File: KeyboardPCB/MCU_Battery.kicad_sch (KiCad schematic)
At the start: 23 parts, among them U1 ATmega32U4-M, U2 TPS61222DCK, U3 MCP73831-2-OT, Y1 XRCGB16M000FXN02R0

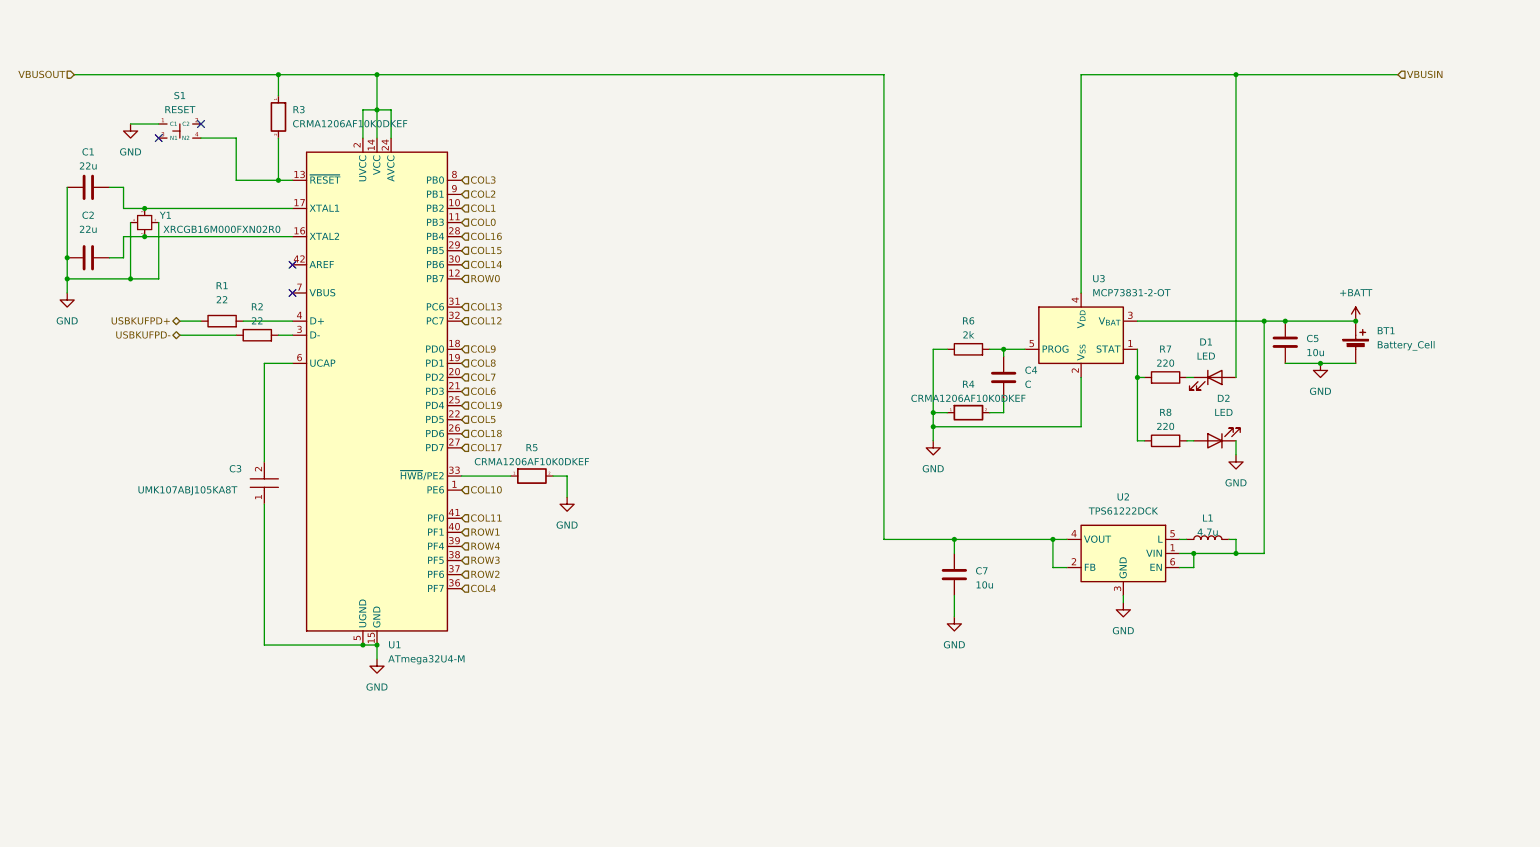
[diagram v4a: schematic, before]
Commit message: Added Symbols and placed them
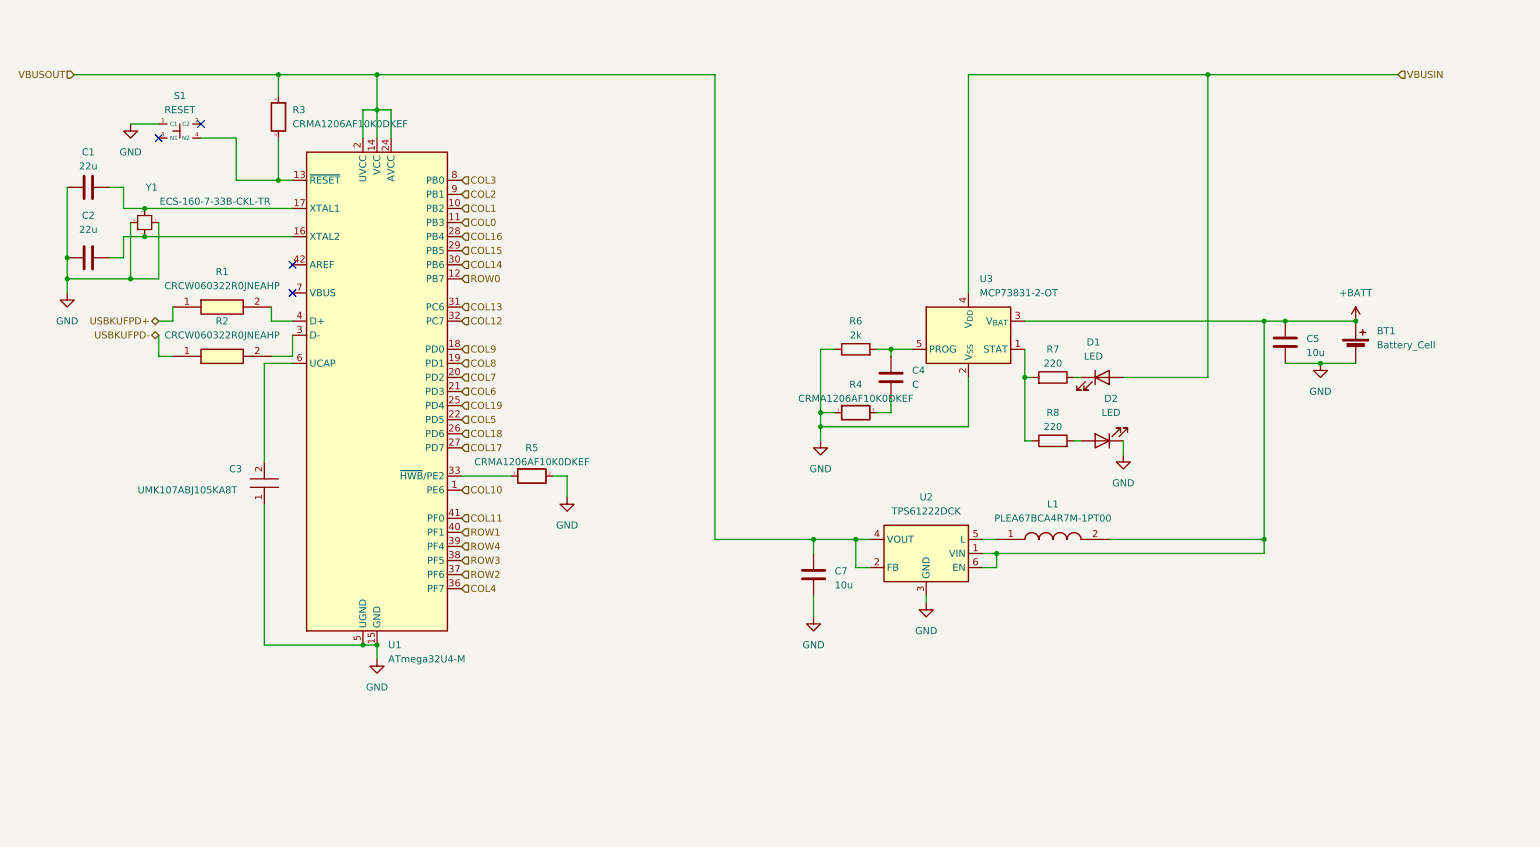
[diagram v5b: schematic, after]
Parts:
- removed L1: 4.7u, symbol Device:L
- removed R1, R2: 22, symbol Device:R
- removed Y1: XRCGB16M000FXN02R0, XRCGB16M000FXN02R0, symbol keyboard_syms:XRCGB16M000FXN02R0
- added L1: PLEA67BCA4R7M-1PT00, keyboard_syms:PLEA67BCA4R7M1PT00, symbol keyboard_syms:PLEA67BCA4R7M-1PT00
- added R1, R2: CRCW060322R0JNEAHP, keyboard_syms:RESC1608X50N, symbol keyboard_syms:CRCW060322R0JNEAHP
- added Y1: ECS-160-7-33B-CKL-TR, keyboard_syms:ECS160733BCKLTR, symbol keyboard_syms:ECS-160-7-33B-CKL-TR
- C3: footprint CAPC1608X95N -> keyboard_syms:CAPC1608X95N
- R3, R4, R5: footprint RESC3216X74N -> keyboard_syms:RESC3216X74N
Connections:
- net +BATT: now also L1.2
- net GND: now also Y1.2, Y1.4
- net USBKUFPD+: now also R1.1
- net USBKUFPD-: now also R2.1
- net at U1.4 (D+): now also R1.2
- net at U2.5 (L): now also L1.1
- net at C2.1, U1.16 (XTAL2): now also Y1.1
- net at C1.1, U1.17 (XTAL1): now also Y1.3
- net at U1.3 (D-): now also R2.2
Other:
- moved on the sheet: C4, C7, D1, D2, R4, R6, R7, R8, U2, U3

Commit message: changed several components
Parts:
- removed C1, C2: 22u, symbol Device:C
- removed C5, C7: 10u, symbol Device:C
- removed D1, D2: LED, symbol Device:LED
- removed R4: CRMA1206AF10K0DKEF, keyboard_syms:RESC3216X74N, symbol keyboard_syms:CRMA1206AF10K0DKEF
- removed R6: 2k, symbol Device:R
- removed R7, R8: 220, symbol Device:R
- removed U2: TPS61222DCK, Package_TO_SOT_SMD:Texas_R-PDSO-G6, symbol Regulator_Switching:TPS61222DCK
- removed U3: MCP73831-2-OT, Package_TO_SOT_SMD:SOT-23-5, symbol Battery_Management:MCP73831-2-OT
- added C1, C2, C7, C8, C9: GRM21BC81C226ME44L, keyboard_syms:CAPC2012X145N, symbol keyboard_syms:GRM21BC81C226ME44L
- added LED1: 150080VS75000, keyboard_syms:LEDC2012X80N, symbol keyboard_syms:150080VS75000
- added R10: CRMA1206AF10K0DKEF, keyboard_syms:RESC3216X74N, symbol keyboard_syms:CRMA1206AF10K0DKEF
- added R4: 330k, symbol Device:R
- added R6: ERJ-H2RD2200X, keyboard_syms:H2C_H2R, symbol keyboard_syms:ERJ-H2RD2200X
- added U2: TPS61236PRWLT, keyboard_syms:TPS61235PRWLT, symbol keyboard_syms:TPS61236PRWLT
- added U3: BQ297xy, Package_SON:WSON-6_1.5x1.5mm_P0.5mm, symbol Battery_Management:BQ297xy
- added U4: BQ24193RGER, keyboard_syms:QFN50P400X400X100-25N-D, symbol keyboard_syms:BQ24193RGER
- C4: value C -> .1u
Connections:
- net +BATT: now also R10.2, R4.1, U2.3 (VIN), U2.7 (EN), U4.13 (BAT_1), U4.14 (BAT_2)
- net GND: now also C1.1, C2.1, C7.2, C8.2, C9.2, R10.1, R6.2, U2.1 (PGND), U2.4 (CC), U2.5 (AGND), U2.8 (INACT), U4.11 (TS1), U4.12 (TS2), U4.17 (PGND_1), U4.18 (PGND_2), U4.2 (PSEL); no longer BT1.2 (-)
- net VBUSIN: now also U4.1 (VBUS_1), U4.24 (VBUS_2)
- net VBUSOUT: now also C7.1, C8.1, C9.1, U2.6 (FB), U2.9 (VOUT)
- net at C4.1: now also R4.2, U3.5 (BAT)
- net -BATT: now reaches C4.2
- net -BATT: now also BT1.2 (-), U3.4 (VSS)
- net at U1.16 (XTAL2), Y1.1: now also C2.2
- net at U1.17 (XTAL1), Y1.3: now also C1.2
- net at L1.1: now also U2.2 (SW)
- new net: LED1.1 (K), R6.1
- new net: LED1.2 (A), U4.3 (~{PG})
- no-connect marks 4 -> 9
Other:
- moved on the sheet: R5, S1, Y1

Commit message: made changes to the board
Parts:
- added C6: 1u, symbol Device:C
- added LED2, LED3, LED4: 150080VS75000, keyboard_syms:LEDC2012X80N, symbol keyboard_syms:150080VS75000
- added LED5: 150060RS75000, keyboard_syms:LEDC1608X80N, symbol keyboard_syms:150060RS75000
- added R11, R7, R8, R9: ERJ-H2RD2200X, keyboard_syms:H2C_H2R, symbol keyboard_syms:ERJ-H2RD2200X
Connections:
- net GND: now also C6.2, LED2.1 (K), R11.2, R7.2, R8.2
- net VBUSIN: now also U4.9 (~{CE}), LED5.2 (A)
- net at U4.10 (ILIM): now also R11.1
- net at U4.19 (SW_1): now also U4.20 (SW_2)
- net at U4.22 (REGN): now also C6.1
- net at U4.23 (PMID): now also LED3.2 (A)
- net at U4.25 (EP): now also LED4.2 (A)
- net at U4.4 (STAT): now also R9.2
- new net: LED4.1 (K), R7.1
- new net: LED3.1 (K), R8.1
- new net: LED2.2 (A), LED5.1 (K), R9.1
- no-connect marks 9 -> 10
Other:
- moved on the sheet: BT1, C1, C2, C3, C4, C7, C8, C9, L1, LED1, R1, R10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

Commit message: Schematic Filled out
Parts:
- removed C6: 1u, symbol Device:C
- added C10: .047u, symbol Device:C
- added C11: UMK107ABJ105KA8T, keyboard_syms:CAPC1608X95N, symbol keyboard_syms:UMK107ABJ105KA8T
- added L2: 2.2u, symbol Device:L
- added Q1, Q2: CSD17527Q5A, Package_TO_SOT_SMD:TDSON-8-1, symbol Transistor_FET:CSD17527Q5A
- added R12: 2.2k, symbol Device:R
- added R13: 2.27k, symbol Device:R
- added R14: 6.86k, symbol Device:R
- added R15, R16: 5M, symbol Device:R
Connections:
- net -BATT: now also Q2.1 (S), Q2.2 (S), Q2.3 (S)
- net GND: now also U4.9 (~{CE}), C11.2, Q1.1 (S), Q1.2 (S), Q1.3 (S), R12.2, R14.2, R15.2; no longer U4.11 (TS1), U4.12 (TS2)
- net VBUSIN: no longer U4.9 (~{CE})
- net at U3.2 (Cout): now also Q1.4 (G), R15.1
- net at U3.3 (Dout): now also Q2.4 (G), R16.1
- net at U3.6 (V-): now also R12.1
- net at U4.22 (REGN): now also C11.1, R13.1
- net at U4.15 (SYS_1): now also U4.16 (SYS_2), L2.2
- net at U4.19 (SW_1), U4.20 (SW_2): now also C10.2
- net at U4.21 (BTST): now also C10.1, L2.1
- new net: Q1.5 (D), Q2.5 (D), R16.2
- new net: R13.2, R14.1, U4.11 (TS1), U4.12 (TS2)
- no-connect marks 10 -> 8
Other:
- moved on the sheet: BT1, C4, L1, R10, R11, R4, U2, U3
